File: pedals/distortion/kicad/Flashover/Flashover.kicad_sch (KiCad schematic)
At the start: 0 parts

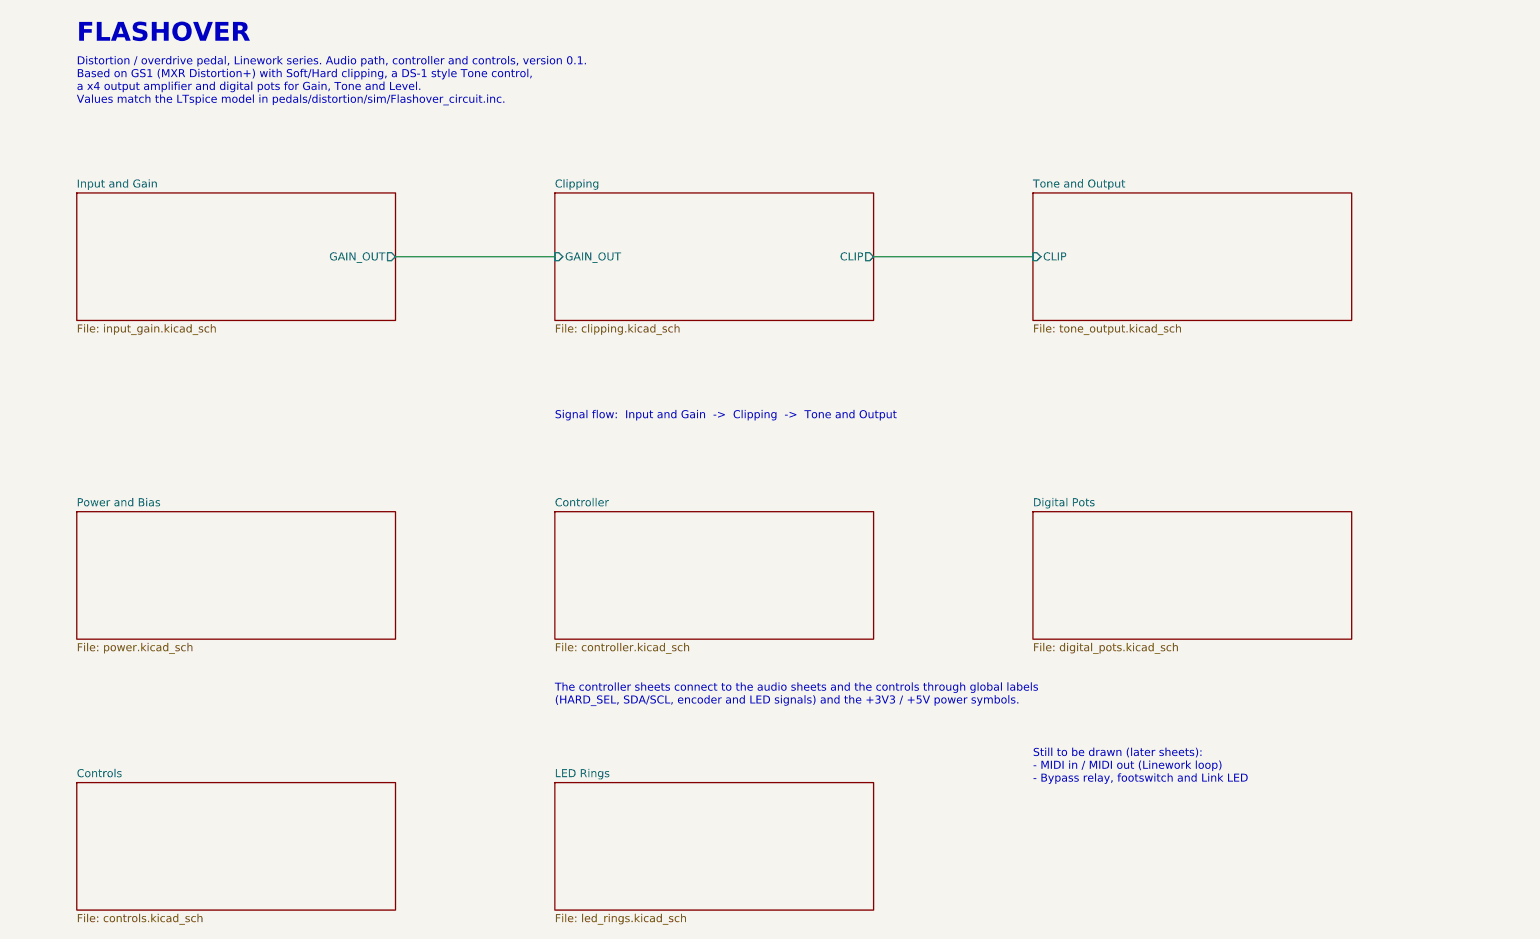
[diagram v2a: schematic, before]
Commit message: Add Flashover MIDI sheet
MIDI in (H11L1 optocoupler, 220 ohm, reverse-protection diode, sleeve
unconnected) and MIDI out (3.3V drive: 33 ohm to pin 4, 10 ohm to pin 5)
on 3.5 mm TRS Type A jacks, wired to UART0. Root sheet re-spaced for
nine sheets. ERC clean.

Co-Authored-By: Claude Opus 5.5 <noreply@anthropic.com>
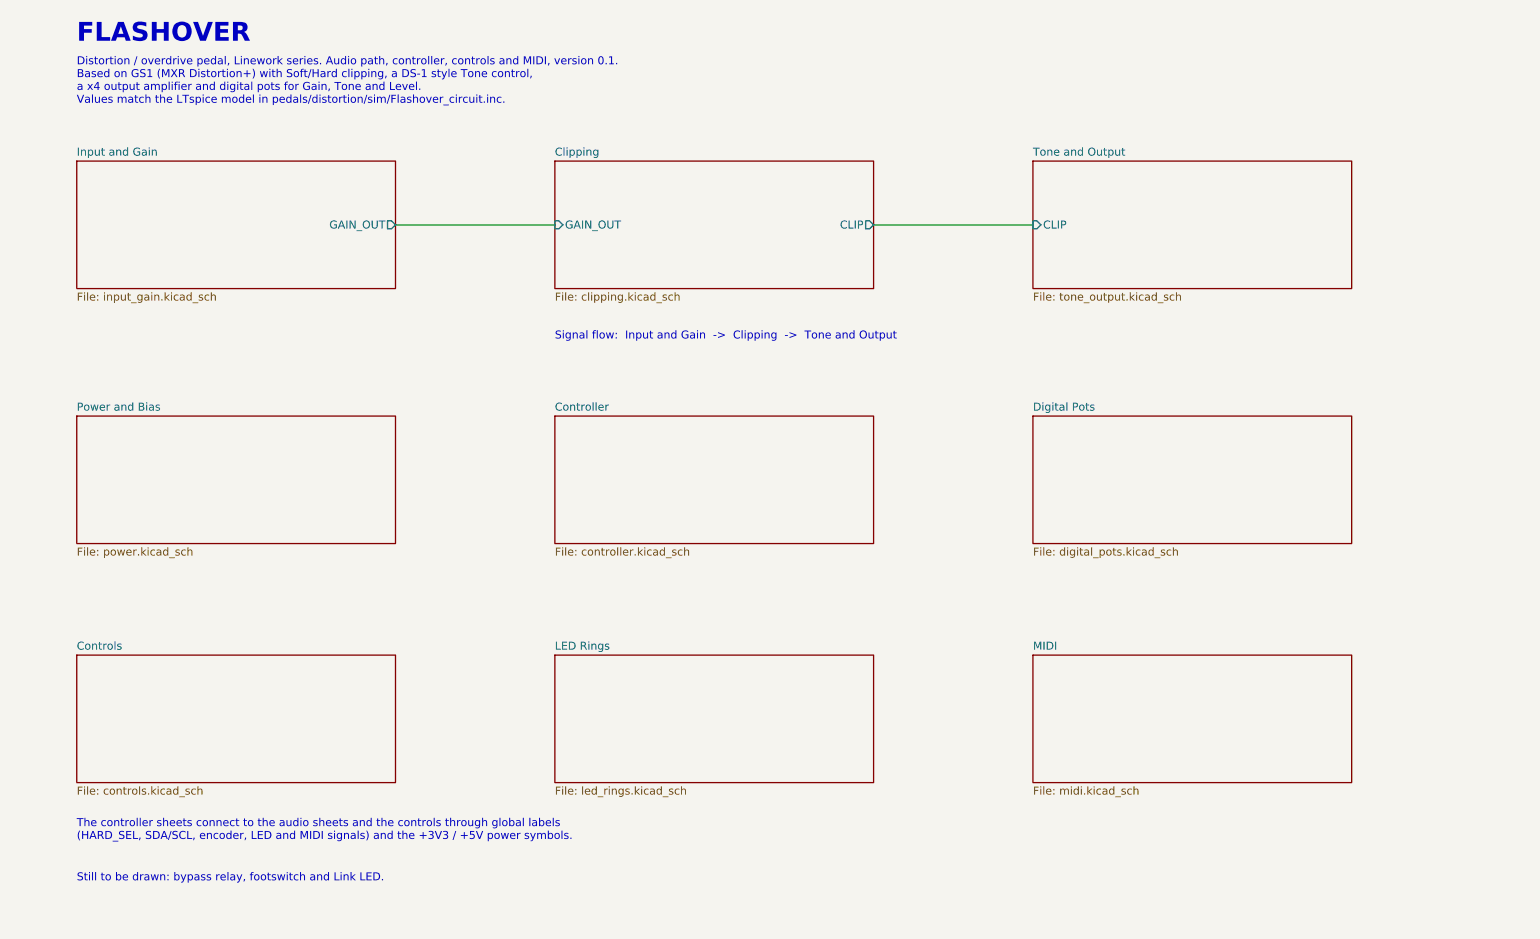
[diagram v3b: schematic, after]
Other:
- added sheet MIDI (midi.kicad_sch)
- note added: "Distortion / overdrive pedal, Linework series. Audio path, controller, controls and MIDI, version 0.1. Based on GS1 (MXR Distortion+) with Soft/Hard clipping, a DS-1 style Tone control, a x4 output amplifier and digital pots for Gain, Tone and Level. Values match the LTspice model in pedals/distortion/sim/Flashover_circuit.inc."
- note added: "Still to be drawn: bypass relay, footswitch and Link LED."
- note added: "The controller sheets connect to the audio sheets and the controls through global labels (HARD_SEL, SDA/SCL, encoder, LED and MIDI signals) and the +3V3 / +5V power symbols."
- note removed: "Distortion / overdrive pedal, Linework series. Audio path, controller and controls, version 0.1. Based on GS1 (MXR Distortion+) with Soft/Hard clipping, a DS-1 style Tone control, a x4 output amplifier and digital pots for Gain, Tone and Level. Values match the LTspice model in pedals/distortion/sim/Flashover_circuit.inc."
- note removed: "Still to be drawn (later sheets): - MIDI in / MIDI out (Linework loop) - Bypass relay, footswitch and Link LED"
- note removed: "The controller sheets connect to the audio sheets and the controls through global labels (HARD_SEL, SDA/SCL, encoder and LED signals) and the +3V3 / +5V power symbols."
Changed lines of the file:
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@@
 	(wire
 		(pts
-			(xy 91.44 73.66) (xy 116.84 73.66)
+			(xy 91.44 68.58) (xy 116.84 68.58)
 		)
 		(stroke
@@
 	(wire
 		(pts
-			(xy 167.64 73.66) (xy 193.04 73.66)
+			(xy 167.64 68.58) (xy 193.04 68.58)
 		)
 		(stroke
@@
 		(effects (font (size 3 3) (bold yes)) (justify left))
 	)
-	(text "Distortion / overdrive pedal, Linework series. Audio path, controller and controls, version 0.1.\nBased on GS1 (MXR Distortion+) with Soft/Hard clipping, a DS-1 style Tone control,\na x4 output amplifier and digital pots for Gain, Tone and Level.\nValues match the LTspice model in pedals/distortion/sim/Flashover_circuit.inc."
+	(text "Distortion / overdrive pedal, Linework series. Audio path, controller, controls and MIDI, version 0.1.\nBased on GS1 (MXR Distortion+) with Soft/Hard clipping, a DS-1 style Tone control,\na x4 output amplifier and digital pots for Gain, Tone and Level.\nValues match the LTspice model in pedals/distortion/sim/Flashover_circuit.inc."
 		(exclude_from_sim no)
 		(at 40.64 45.72 0)
@@
 	(text "Signal flow:  Input and Gain  ->  Clipping  ->  Tone and Output"
 		(exclude_from_sim no)
-		(at 116.84 99.06 0)
+		(at 116.84 86.36 0)
 		(effects (font (size 1.27 1.27)) (justify left))
 	)
-	(text "The controller sheets connect to the audio sheets and the controls through global labels\n(HARD_SEL, SDA/SCL, encoder and LED signals) and the +3V3 / +5V power symbols."
-		(exclude_from_sim no)
-		(at 116.84 143.51 0)
+	(text "The controller sheets connect to the audio sheets and the controls through global labels\n(HARD_SEL, SDA/SCL, encoder, LED and MIDI signals) and the +3V3 / +5V power symbols."
+		(exclude_from_sim no)
+		(at 40.64 165.1 0)
 		(effects (font (size 1.27 1.27)) (justify left))
 	)
-	(text "Still to be drawn (later sheets):\n- MIDI in / MIDI out (Linework loop)\n- Bypass relay, footswitch and Link LED"
-		(exclude_from_sim no)
-		(at 193.04 154.94 0)
+	(text "Still to be drawn: bypass relay, footswitch and Link LED."
+		(exclude_from_sim no)
+		(at 40.64 172.72 0)
 		(effects (font (size 1.27 1.27)) (justify left))
 	)
 	(sheet
-		(at 40.64 114.3)
+		(at 40.64 99.06)
 		(size 50.8 20.32)
 		(exclude_from_sim no)
@@
 		)
 		(property "Sheetname" "Power and Bias"
-			(at 40.64 113.5884 0)
+			(at 40.64 98.3484 0)
 			(show_name no)
 			(do_not_autoplace no)
@@
 		)
 		(property "Sheetfile" "power.kicad_sch"
-			(at 40.64 135.2046 0)
-			(show_name no)
-			(do_not_autoplace no)
-			(effects (font (size 1.27 1.27)) (justify left top))
-		)
-		(instances
-			(project "Flashover"
-				(path "/ea9f0b88-0903-4174-9c8e-623c203001c6"
+			(at 40.64 119.9646 0)
+			(show_name no)
+			(do_not_autoplace no)
+			(effects (font (size 1.27 1.27)) (justify left top))
+		)
+		(instances
+			(project "Flashover"
+				(path "/6aa723b4-171b-4dbf-8521-b922c86d1498"
 					(page "2")
 				)
@@
 	)
 	(sheet
-		(at 40.64 63.5)
+		(at 40.64 58.42)
 		(size 50.8 20.32)
 		(exclude_from_sim no)
@@
 		)
 		(property "Sheetname" "Input and Gain"
-			(at 40.64 62.7884 0)
+			(at 40.64 57.7084 0)
 			(show_name no)
 			(do_not_autoplace no)
@@
 		)
 		(property "Sheetfile" "input_gain.kicad_sch"
-			(at 40.64 84.4046 0)
+			(at 40.64 79.3246 0)
 			(show_name no)
 			(do_not_autoplace no)
@@
 		)
 		(pin "GAIN_OUT" output
-			(at 91.44 73.66 0)
+			(at 91.44 68.58 0)
 			(effects (font (size 1.27 1.27)) (justify right))
 		)
 		(instances
 			(project "Flashover"
-				(path "/ea9f0b88-0903-4174-9c8e-623c203001c6"
+				(path "/6aa723b4-171b-4dbf-8521-b922c86d1498"
 					(page "3")
 				)
@@
 	)
 	(sheet
-		(at 116.84 63.5)
+		(at 116.84 58.42)
 		(size 50.8 20.32)
 		(exclude_from_sim no)
@@
 		)
 		(property "Sheetname" "Clipping"
-			(at 116.84 62.7884 0)
+			(at 116.84 57.7084 0)
 			(show_name no)
 			(do_not_autoplace no)
@@
 		)
 		(property "Sheetfile" "clipping.kicad_sch"
-			(at 116.84 84.4046 0)
+			(at 116.84 79.3246 0)
 			(show_name no)
 			(do_not_autoplace no)
@@
 		)
 		(pin "GAIN_OUT" input
-			(at 116.84 73.66 180)
+			(at 116.84 68.58 180)
 			(effects (font (size 1.27 1.27)) (justify left))
 		)
 		(pin "CLIP" output
-			(at 167.64 73.66 0)
+			(at 167.64 68.58 0)
 			(effects (font (size 1.27 1.27)) (justify right))
 		)
 		(instances
 			(project "Flashover"
-				(path "/ea9f0b88-0903-4174-9c8e-623c203001c6"
+				(path "/6aa723b4-171b-4dbf-8521-b922c86d1498"
 					(page "4")
 				)
@@
 	)
 	(sheet
-		(at 193.04 63.5)
+		(at 193.04 58.42)
 		(size 50.8 20.32)
 		(exclude_from_sim no)
@@
 		)
 		(property "Sheetname" "Tone and Output"
-			(at 193.04 62.7884 0)
+			(at 193.04 57.7084 0)
 			(show_name no)
 			(do_not_autoplace no)
@@
 		)
 		(property "Sheetfile" "tone_output.kicad_sch"
-			(at 193.04 84.4046 0)
+			(at 193.04 79.3246 0)
 			(show_name no)
 			(do_not_autoplace no)
@@
 		)
 		(pin "CLIP" input
-			(at 193.04 73.66 180)
+			(at 193.04 68.58 180)
 			(effects (font (size 1.27 1.27)) (justify left))
 		)
 		(instances
 			(project "Flashover"
-				(path "/ea9f0b88-0903-4174-9c8e-623c203001c6"
+				(path "/6aa723b4-171b-4dbf-8521-b922c86d1498"
 					(page "5")
 				)
@@
 	)
 	(sheet
-		(at 116.84 114.3)
+		(at 116.84 99.06)
 		(size 50.8 20.32)
 		(exclude_from_sim no)
@@
 		)
 		(property "Sheetname" "Controller"
-			(at 116.84 113.5884 0)
+			(at 116.84 98.3484 0)
 			(show_name no)
 			(do_not_autoplace no)
@@
 		)
 		(property "Sheetfile" "controller.kicad_sch"
-			(at 116.84 135.2046 0)
-			(show_name no)
-			(do_not_autoplace no)
-			(effects (font (size 1.27 1.27)) (justify left top))
-		)
-		(instances
-			(project "Flashover"
-				(path "/ea9f0b88-0903-4174-9c8e-623c203001c6"
+			(at 116.84 119.9646 0)
+			(show_name no)
+			(do_not_autoplace no)
+			(effects (font (size 1.27 1.27)) (justify left top))
+		)
+		(instances
+			(project "Flashover"
+				(path "/6aa723b4-171b-4dbf-8521-b922c86d1498"
 					(page "6")
 				)
@@
 	)
 	(sheet
-		(at 193.04 114.3)
+		(at 193.04 99.06)
 		(size 50.8 20.32)
 		(exclude_from_sim no)
@@
 		)
 		(property "Sheetname" "Digital Pots"
-			(at 193.04 113.5884 0)
+			(at 193.04 98.3484 0)
 			(show_name no)
 			(do_not_autoplace no)
@@
 		)
 		(property "Sheetfile" "digital_pots.kicad_sch"
-			(at 193.04 135.2046 0)
-			(show_name no)
-			(do_not_autoplace no)
-			(effects (font (size 1.27 1.27)) (justify left top))
-		)
-		(instances
-			(project "Flashover"
-				(path "/ea9f0b88-0903-4174-9c8e-623c203001c6"
+			(at 193.04 119.9646 0)
+			(show_name no)
+			(do_not_autoplace no)
+			(effects (font (size 1.27 1.27)) (justify left top))
+		)
+		(instances
+			(project "Flashover"
+				(path "/6aa723b4-171b-4dbf-8521-b922c86d1498"
 					(page "7")
 				)
@@
 	)
 	(sheet
-		(at 40.64 157.48)
+		(at 40.64 137.16)
 		(size 50.8 20.32)
 		(exclude_from_sim no)
@@
 		)
 		(property "Sheetname" "Controls"
-			(at 40.64 156.7684 0)
+			(at 40.64 136.4484 0)
 			(show_name no)
 			(do_not_autoplace no)
@@
 		)
 		(property "Sheetfile" "controls.kicad_sch"
-			(at 40.64 178.3846 0)
-			(show_name no)
-			(do_not_autoplace no)
-			(effects (font (size 1.27 1.27)) (justify left top))
-		)
-		(instances
-			(project "Flashover"
-				(path "/ea9f0b88-0903-4174-9c8e-623c203001c6"
+			(at 40.64 158.0646 0)
+			(show_name no)
+			(do_not_autoplace no)
+			(effects (font (size 1.27 1.27)) (justify left top))
+		)
+		(instances
+			(project "Flashover"
+				(path "/6aa723b4-171b-4dbf-8521-b922c86d1498"
 					(page "8")
 				)
@@
 	)
 	(sheet
-		(at 116.84 157.48)
+		(at 116.84 137.16)
 		(size 50.8 20.32)
 		(exclude_from_sim no)
@@
 		)
 		(property "Sheetname" "LED Rings"
-			(at 116.84 156.7684 0)
+			(at 116.84 136.4484 0)
 			(show_name no)
 			(do_not_autoplace no)
@@
 		)
 		(property "Sheetfile" "led_rings.kicad_sch"
-			(at 116.84 178.3846 0)
-			(show_name no)
-			(do_not_autoplace no)
-			(effects (font (size 1.27 1.27)) (justify left top))
-		)
-		(instances
-			(project "Flashover"
-				(path "/ea9f0b88-0903-4174-9c8e-623c203001c6"
+			(at 116.84 158.0646 0)
+			(show_name no)
+			(do_not_autoplace no)
+			(effects (font (size 1.27 1.27)) (justify left top))
+		)
+		(instances
+			(project "Flashover"
+				(path "/6aa723b4-171b-4dbf-8521-b922c86d1498"
 					(page "9")
 				)
 			)
+		)
+	)
+	(sheet
+		(at 193.04 137.16)
+		(size 50.8 20.32)
+		(exclude_from_sim no)
+		(in_bom yes)
+		(on_board yes)
+		(dnp no)
+		(fields_autoplaced yes)
+		(stroke
+			(width 0.1524)
+			(type solid)
+		)
+		(fill
+			(color 0 0 0 0.0000)
+		)
+		(property "Sheetname" "MIDI"
+			(at 193.04 136.4484 0)
+			(show_name no)
+			(do_not_autoplace no)
+			(effects (font (size 1.27 1.27)) (justify left bottom))
+		)
+		(property "Sheetfile" "midi.kicad_sch"
+			(at 193.04 158.0646 0)
+			(show_name no)
+			(do_not_autoplace no)
+			(effects (font (size 1.27 1.27)) (justify left top))
+		)
+		(instances
+			(project "Flashover"
+				(path "/6aa723b4-171b-4dbf-8521-b922c86d1498"
+					(page "10")
+				)
+			)
